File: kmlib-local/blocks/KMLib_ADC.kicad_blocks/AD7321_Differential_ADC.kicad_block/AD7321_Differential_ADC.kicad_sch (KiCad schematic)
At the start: 14 parts, among them U1 PDM1-S24-D15-S, U2 AD7321

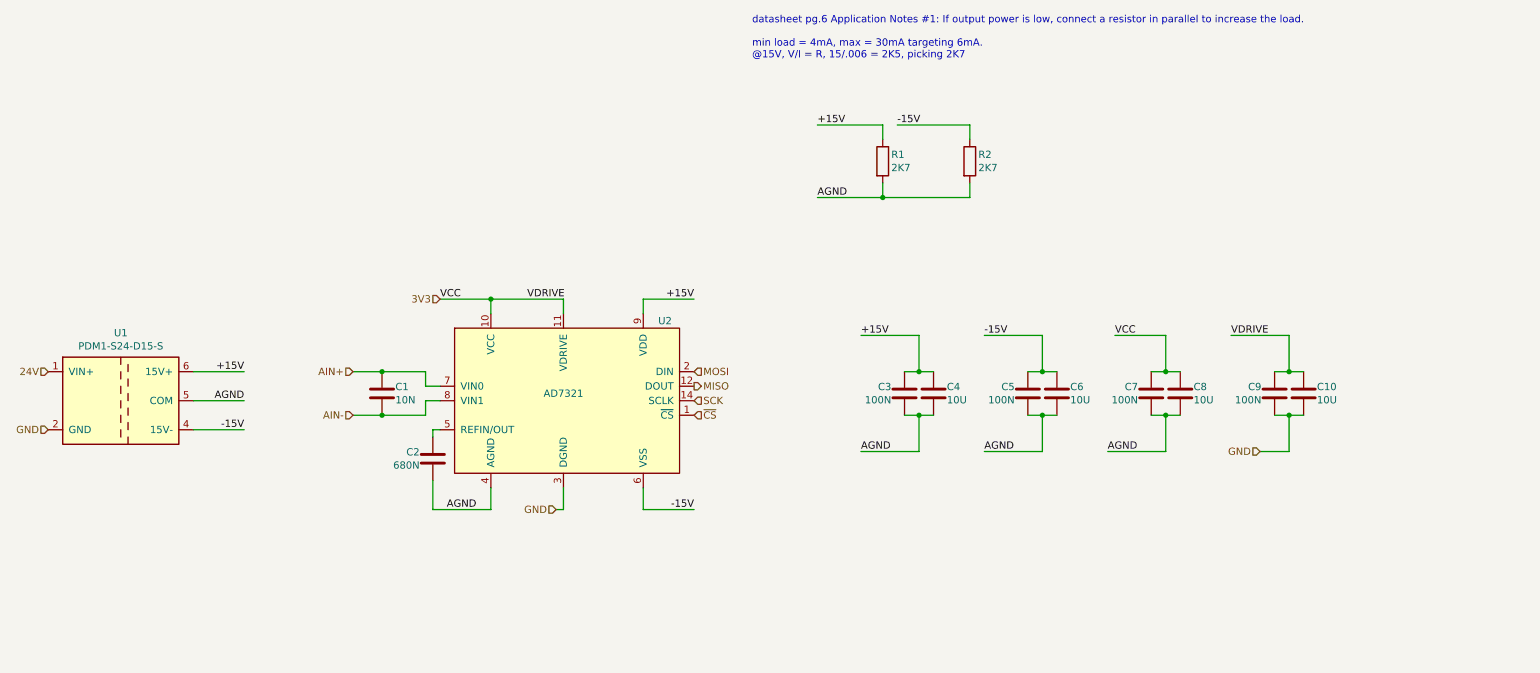
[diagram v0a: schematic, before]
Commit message: rename to use underscores
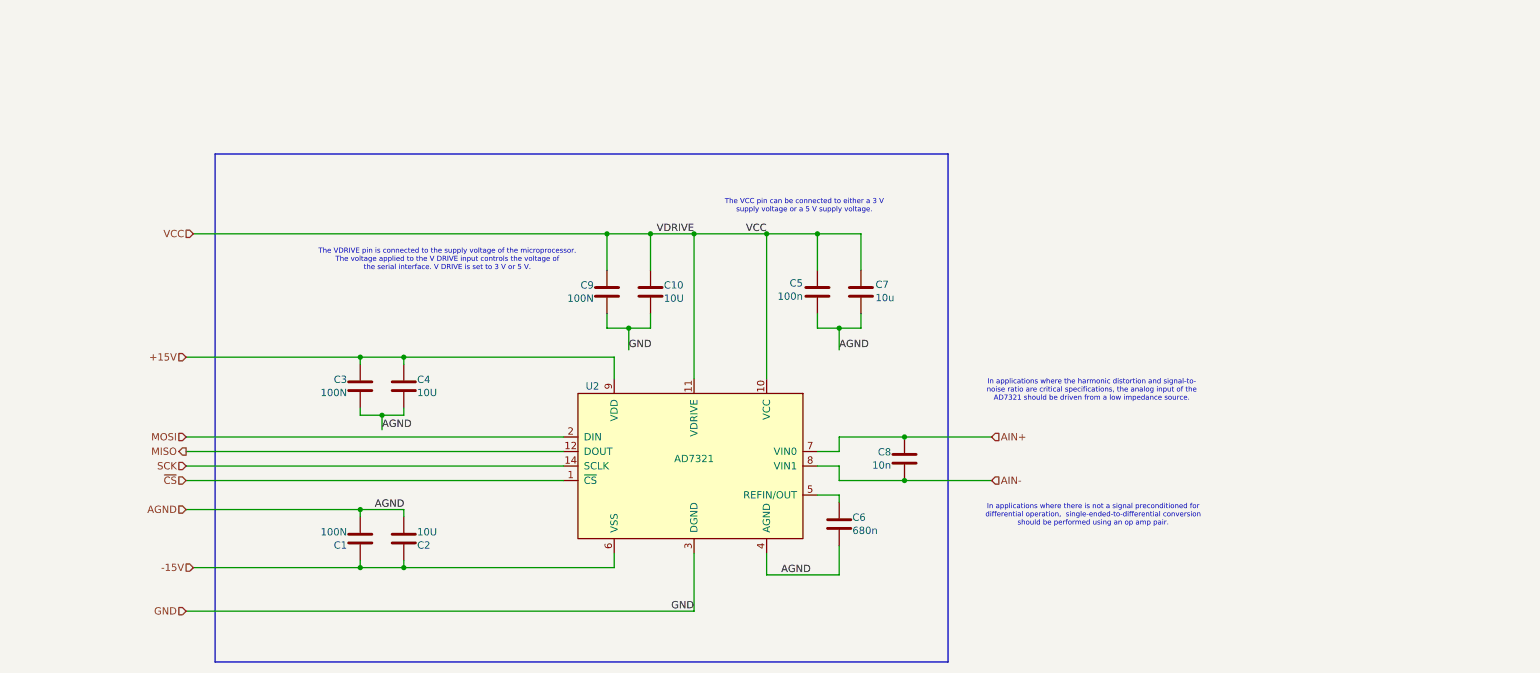
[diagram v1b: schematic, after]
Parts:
- removed R1, R2: 2K7, Resistor_SMD:R_0603_1608Metric, symbol Device:R
- removed U1: PDM1-S24-D15-S, william_dc_dc:PDM1-XXX-DXX-S, symbol william_dc_dc:PDM1-S24-D15-S
- C5: renamed from C7; value 100N -> 100n
- C6: renamed from C2; value 680N -> 680n
- C7: renamed from C8; value 10U -> 10u
- C8: renamed from C1; value 10N -> 10n
- renumbered C3 to C1, C4 to C2, C5 to C3, C6 to C4
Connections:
- net +15V: now also C3.2, C4.2; no longer C1.2, C2.2
- net -15V: now also C1.2, C2.2; no longer C3.2, C4.2
- net 3V3 renamed VCC
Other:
- note added: "In applications where the harmonic distortion and signal-to- noise ratio are critical specifications, the analog input of the AD7321 should be driven from a low impedance source."
- note added: "In applications where there is not a signal preconditioned for differential operation, single-ended-to-differential conversion should be performed using an op amp pair."
- note added: "The VCC pin can be connected to either a 3 V supply voltage or a 5 V supply voltage."
- note added: "The VDRIVE pin is connected to the supply voltage of the microprocessor. The voltage applied to the V DRIVE input controls the voltage of the serial interface. V DRIVE is set to 3 V or 5 V."
- note removed: "datasheet pg.6 Application Notes #1: If output power is low, connect a resistor in parallel to increase the load. min load = 4mA, max = 30mA targeting 6mA. @15V, V/I = R, 15/.006 = 2K5, picking 2K7"
- moved on the sheet: C1, C10, C2, C3, C4, C5, C6, C7, C8, C9, U2
